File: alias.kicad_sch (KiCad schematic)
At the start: 0 parts

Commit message: Changed PCB Schematic (Part 1 - Not Finished)
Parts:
- added C? (x3): 0.1uF, symbol Device:C_Small
- added C?: 10uF, symbol Device:C_Small
- added C?: 1uF, symbol Device:C_Small
- added C? (x2): 22pF, symbol Device:C_Small
- added R? (x2): 22, symbol Device:R_Small
- added R?: 10k, symbol Device:R_Small
- added U?: ATmega32U4-A, Package_QFP:TQFP-44_10x10mm_P0.8mm, symbol MCU_Microchip_ATmega:ATmega32U4-A
- added Y?: 16MHz, symbol Device:Crystal_GND24_Small
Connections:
- new net: R?.2, U?.3 (D-)
- new net: R?.2, U?.4 (D+)
- new net: R?.1, U?.33 (~{HWB}/PE2)
- new net: C?.2, U?.17 (XTAL1), Y?.1
- new net: C?.2, U?.16 (XTAL2), Y?.3
- new net: C?.1, U?.6 (UCAP)
- new net +5V: C?.1, C?.1, C?.1, C?.1, U?.14 (VCC), U?.2 (UVCC), U?.24 (AVCC), U?.34 (VCC), U?.44 (AVCC), U?.7 (VBUS)
- new net GND: C?.1, C?.1, C?.2, C?.2, C?.2, C?.2, C?.2, R?.2, U?.15 (GND), U?.23 (GND), U?.35 (GND), U?.43 (GND), U?.5 (UGND), Y?.2

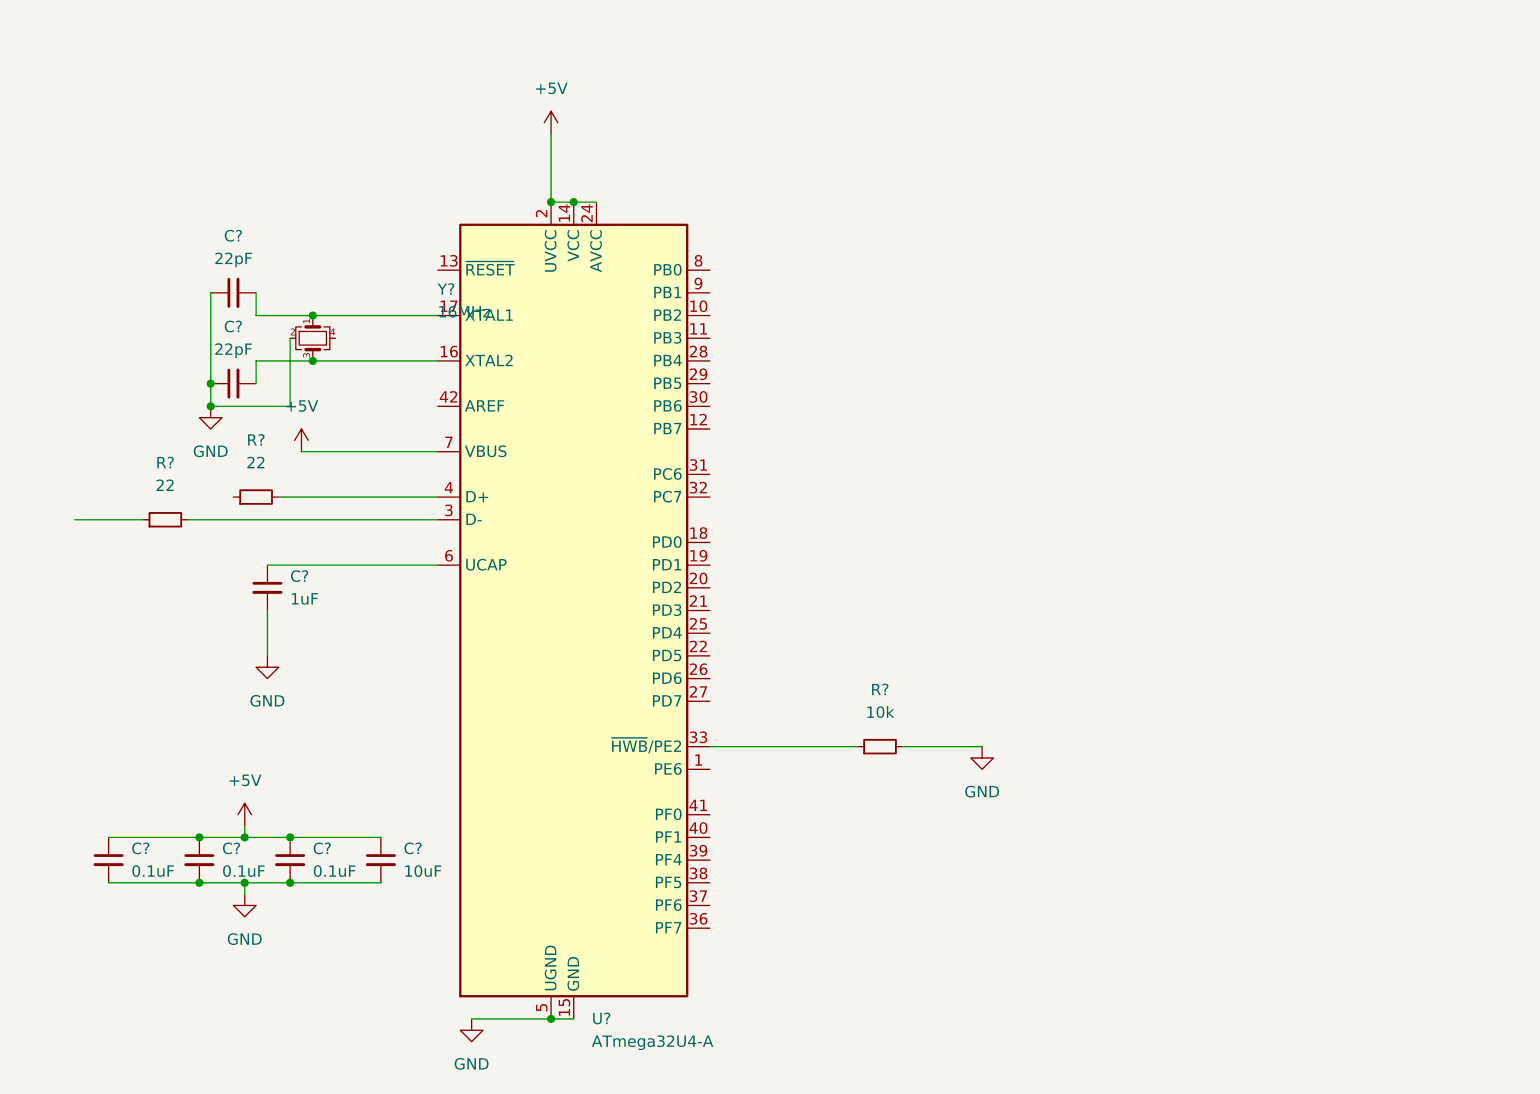
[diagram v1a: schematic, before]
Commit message: Finished PCB Schematic
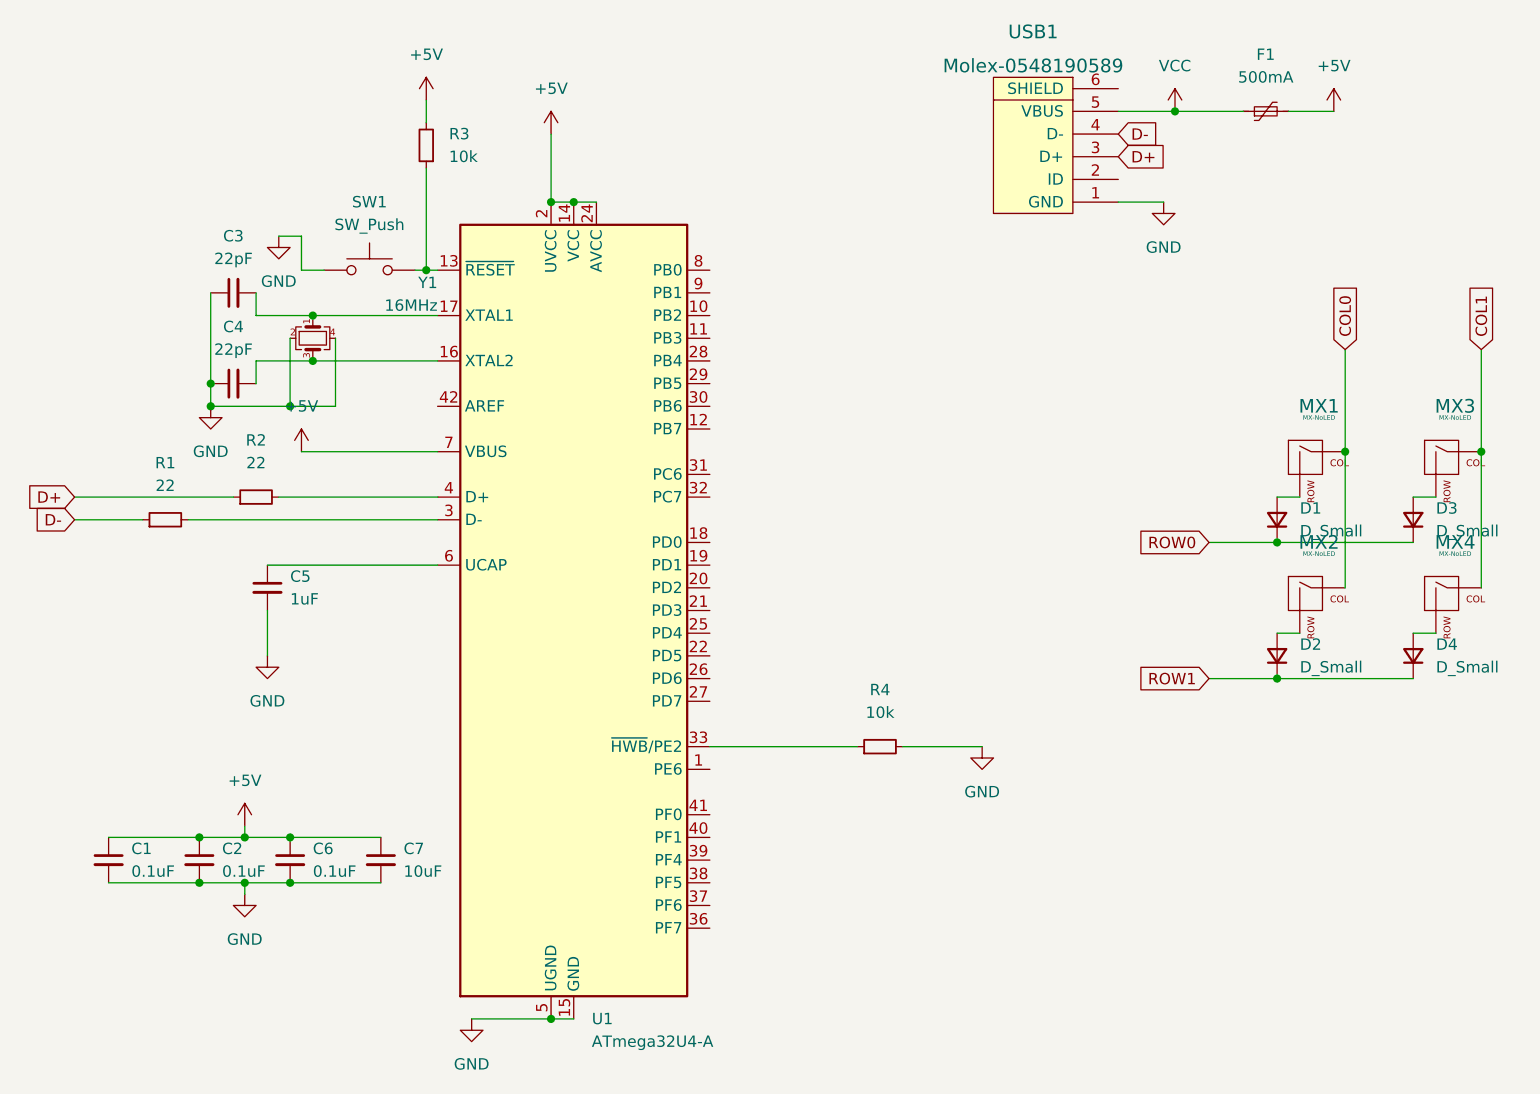
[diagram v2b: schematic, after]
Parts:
- added D1, D2, D3, D4: D_Small, Diode_SMD:D_SOD-123, symbol Device:D_Small
- added F1: 500mA, Fuse:Fuse_1206_3216Metric, symbol Device:Polyfuse_Small
- added MX1, MX2, MX3, MX4: MX-NoLED, MX_Only:MXOnly-1U-NoLED, symbol MX_Alps_Hybrid:MX-NoLED
- added R3: 10k, Resistor_SMD:R_0805_2012Metric, symbol Device:R_Small
- added SW1: SW_Push, random-keyboard-parts:SKQG-1155865, symbol Switch:SW_Push
- added USB1: Molex-0548190589, random-keyboard-parts:Molex-0548190589, symbol random-keyboard-parts:Molex-0548190589
- C1, C2, C3, C4, C5, C6, C7: renamed from C?; footprint (none) -> Capacitor_SMD:C_0805_2012Metric
- R1, R2, R4: renamed from R?; footprint (none) -> Resistor_SMD:R_0805_2012Metric
- Y1: renamed from Y?; footprint (none) -> Crystal:Crystal_SMD_3225-4Pin_3.2x2.5mm
- gave numbers to parts that had none: 1
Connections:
- net +5V: now also F1.2, R3.2
- net GND: now also Y1.4, SW1.1, USB1.1 (GND)
- net D-: now reaches R1.1
- net D-: now also USB1.4 (D-)
- net D+: now reaches R2.1
- net D+: now also USB1.3 (D+)
- net at U1.13 (~{RESET}): now also R3.1, SW1.2
- new net: D3.2 (A), MX3.2 (ROW)
- new net: D4.2 (A), MX4.2 (ROW)
- new net: D1.2 (A), MX1.2 (ROW)
- new net: D2.2 (A), MX2.2 (ROW)
- new net COL0: MX1.1 (COL), MX2.1 (COL)
- new net COL1: MX3.1 (COL), MX4.1 (COL)
- new net ROW0: D1.1 (K), D3.1 (K)
- new net ROW1: D2.1 (K), D4.1 (K)
- new net VCC: F1.1, USB1.5 (VBUS)

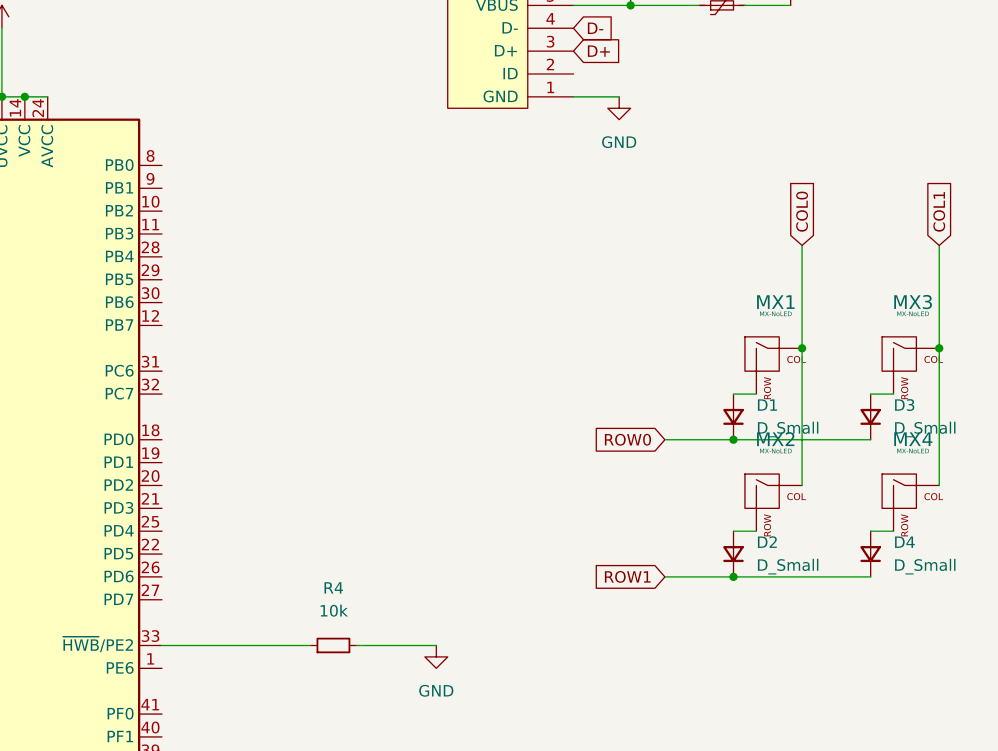
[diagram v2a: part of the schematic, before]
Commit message: Added routing (not finished)
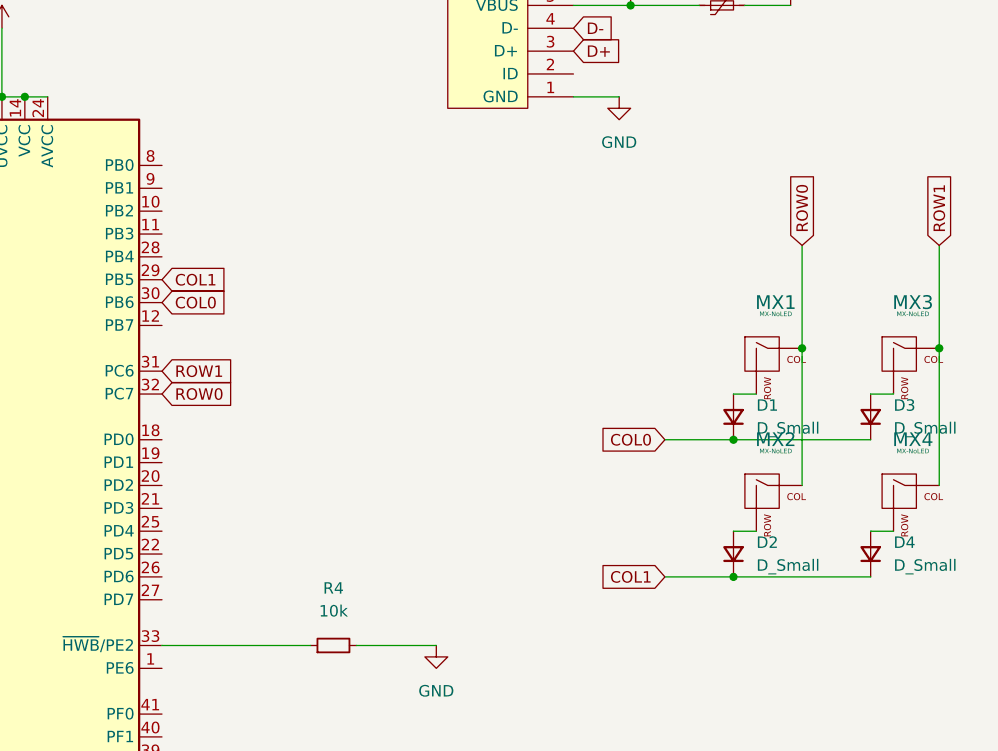
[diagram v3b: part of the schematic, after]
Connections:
- net COL0: now also D1.1 (K), D3.1 (K), U1.30 (PB6); no longer MX1.1 (COL), MX2.1 (COL)
- net COL1: now also D2.1 (K), D4.1 (K), U1.29 (PB5); no longer MX3.1 (COL), MX4.1 (COL)
- net ROW0: now also MX1.1 (COL), MX2.1 (COL), U1.32 (PC7); no longer D1.1 (K), D3.1 (K)
- net ROW1: now also MX3.1 (COL), MX4.1 (COL), U1.31 (PC6); no longer D2.1 (K), D4.1 (K)
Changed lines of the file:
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@@
     )
   )
-  (global_label "COL0" (shape input) (at 173.99 68.58 90) (fields_autoplaced)
+  (global_label "ROW0" (shape input) (at 173.99 68.58 90) (fields_autoplaced)
     (effects (font (size 1.27 1.27)) (justify left))
-    (property "Intersheet References" "${INTERSHEET_REFS}" (id 0) (at 173.9106 61.3288 90)
+    (property "Intersheet References" "${INTERSHEET_REFS}" (id 0) (at 173.9106 60.9055 90)
       (effects (font (size 1.27 1.27)) (justify left) hide)
     )
   )
-  (global_label "ROW0" (shape input) (at 158.75 90.17 180) (fields_autoplaced)
+  (global_label "COL0" (shape input) (at 158.75 90.17 180) (fields_autoplaced)
     (effects (font (size 1.27 1.27)) (justify right))
-    (property "Intersheet References" "${INTERSHEET_REFS}" (id 0) (at 151.0755 90.0906 0)
+    (property "Intersheet References" "${INTERSHEET_REFS}" (id 0) (at 151.4988 90.0906 0)
       (effects (font (size 1.27 1.27)) (justify right) hide)
     )
@@
     )
   )
+  (global_label "COL0" (shape input) (at 102.87 74.93 0) (fields_autoplaced)
+    (effects (font (size 1.27 1.27)) (justify left))
+    (property "Intersheet References" "${INTERSHEET_REFS}" (id 0) (at 110.1212 74.8506 0)
+      (effects (font (size 1.27 1.27)) (justify left) hide)
+    )
+  )
   (global_label "D-" (shape input) (at 148.59 44.45 0) (fields_autoplaced)
     (effects (font (size 1.27 1.27)) (justify left))
@@
     )
   )
-  (global_label "COL1" (shape input) (at 189.23 68.58 90) (fields_autoplaced)
+  (global_label "COL1" (shape input) (at 102.87 72.39 0) (fields_autoplaced)
     (effects (font (size 1.27 1.27)) (justify left))
-    (property "Intersheet References" "${INTERSHEET_REFS}" (id 0) (at 189.1506 61.3288 90)
+    (property "Intersheet References" "${INTERSHEET_REFS}" (id 0) (at 110.1212 72.3106 0)
+      (effects (font (size 1.27 1.27)) (justify left) hide)
+    )
+  )
+  (global_label "ROW1" (shape input) (at 189.23 68.58 90) (fields_autoplaced)
+    (effects (font (size 1.27 1.27)) (justify left))
+    (property "Intersheet References" "${INTERSHEET_REFS}" (id 0) (at 189.1506 60.9055 90)
       (effects (font (size 1.27 1.27)) (justify left) hide)
     )
@@
     )
   )
-  (global_label "ROW1" (shape input) (at 158.75 105.41 180) (fields_autoplaced)
+  (global_label "ROW0" (shape input) (at 102.87 85.09 0) (fields_autoplaced)
+    (effects (font (size 1.27 1.27)) (justify left))
+    (property "Intersheet References" "${INTERSHEET_REFS}" (id 0) (at 110.5445 85.0106 0)
+      (effects (font (size 1.27 1.27)) (justify left) hide)
+    )
+  )
+  (global_label "COL1" (shape input) (at 158.75 105.41 180) (fields_autoplaced)
     (effects (font (size 1.27 1.27)) (justify right))
-    (property "Intersheet References" "${INTERSHEET_REFS}" (id 0) (at 151.0755 105.3306 0)
+    (property "Intersheet References" "${INTERSHEET_REFS}" (id 0) (at 151.4988 105.3306 0)
       (effects (font (size 1.27 1.27)) (justify right) hide)
     )
   )
+  (global_label "ROW1" (shape input) (at 102.87 82.55 0) (fields_autoplaced)
+    (effects (font (size 1.27 1.27)) (justify left))
+    (property "Intersheet References" "${INTERSHEET_REFS}" (id 0) (at 110.5445 82.4706 0)
+      (effects (font (size 1.27 1.27)) (justify left) hide)
+    )
+  )
